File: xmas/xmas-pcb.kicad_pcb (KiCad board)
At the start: 2 copper layers, 45.7 x 88.3 mm, 23 parts, among them J1 ICSP, J2 UART, J3 GPIOs, J4 I2C, J5 USB_A, U1 ATmega328P-AU, U10 WS2811B, U11 WS2811B, U2 WS2811B, U3 WS2811B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

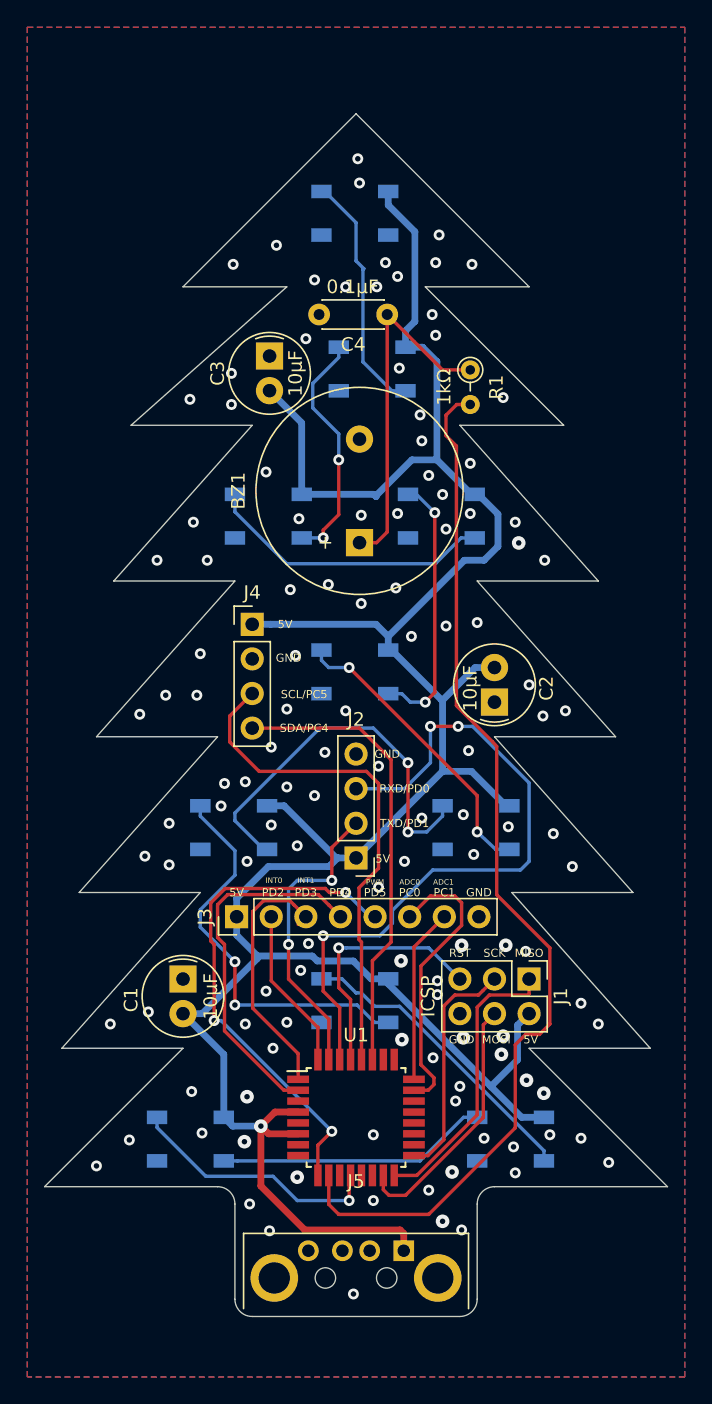
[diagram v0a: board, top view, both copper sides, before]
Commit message: treewide: Update to KiCAD 7
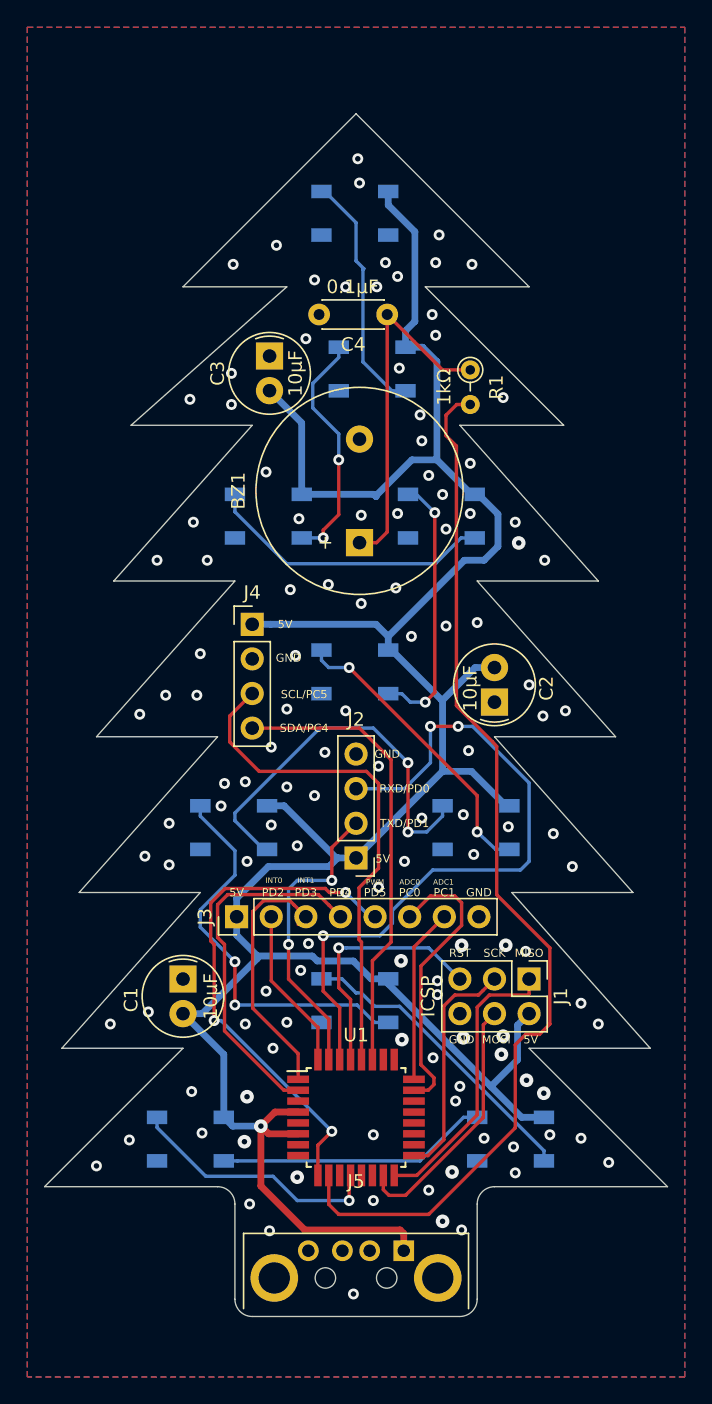
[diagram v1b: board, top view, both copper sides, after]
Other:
- outline, holes or cut-outs redrawn
- net class Default removed
- net class Power removed
